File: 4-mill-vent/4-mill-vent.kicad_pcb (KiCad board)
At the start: 2 copper layers, 76.2 x 47.6 mm, 73 parts, among them J1 Fan, J2 Buzzer, J3 Power, J4 ICSP, Q1 MMBT3904, Q2 MMBT3904, Q3 PZT3904, Q4 PZT3904, Q5 TSM480P06CP, Q6 MMBT3904, SW1 Power_off, SW2 Power_On, SW3 Fan_Down, SW4 Fan_Up, U1 LM321, U2 TPSM84212EAB, U3 LM1117-5.0, U4 ATmega328P-AU, Y1 16.000MHZ

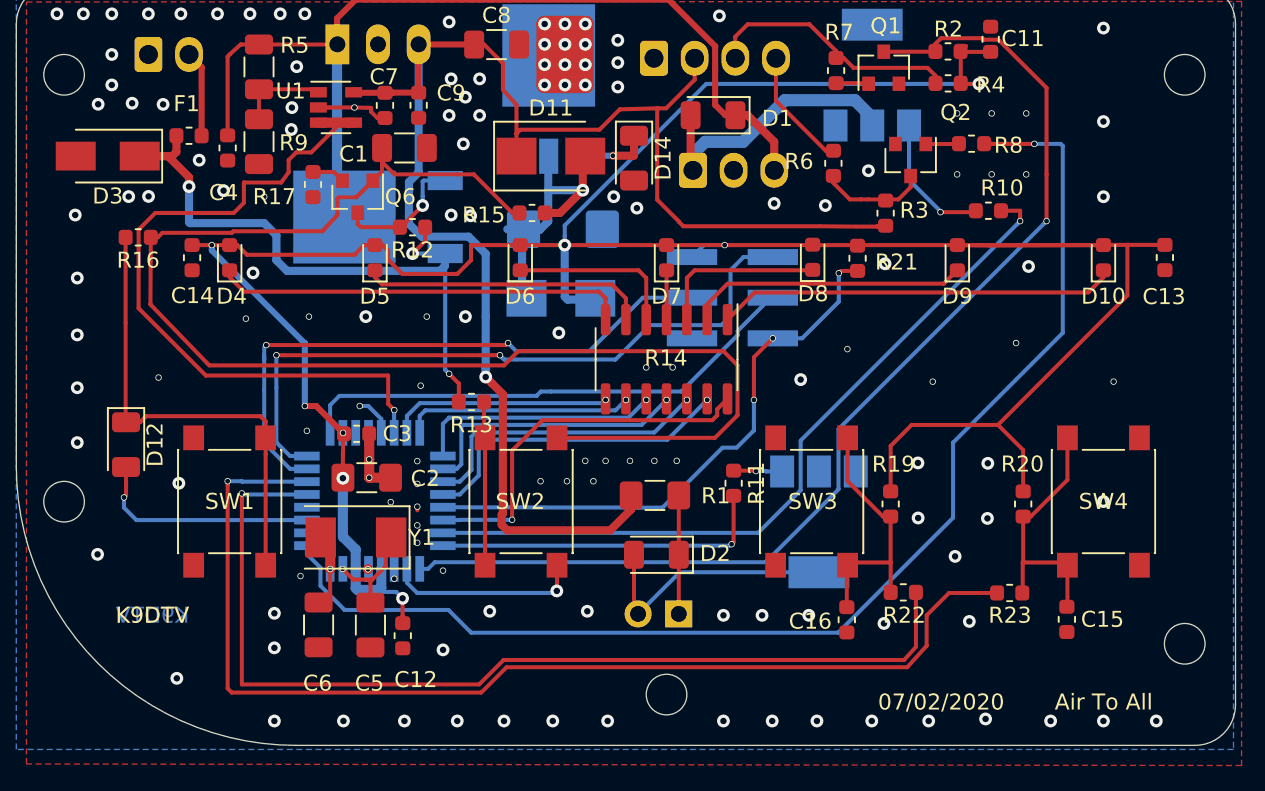
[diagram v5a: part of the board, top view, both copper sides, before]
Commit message: Added more to design
Had to add a transitor for allow the micro to power down the unit.
The reason is Q6's base can be as high as 16v when the on button is pressed.
This micro does not have open collector outputs and that would blow the chip.
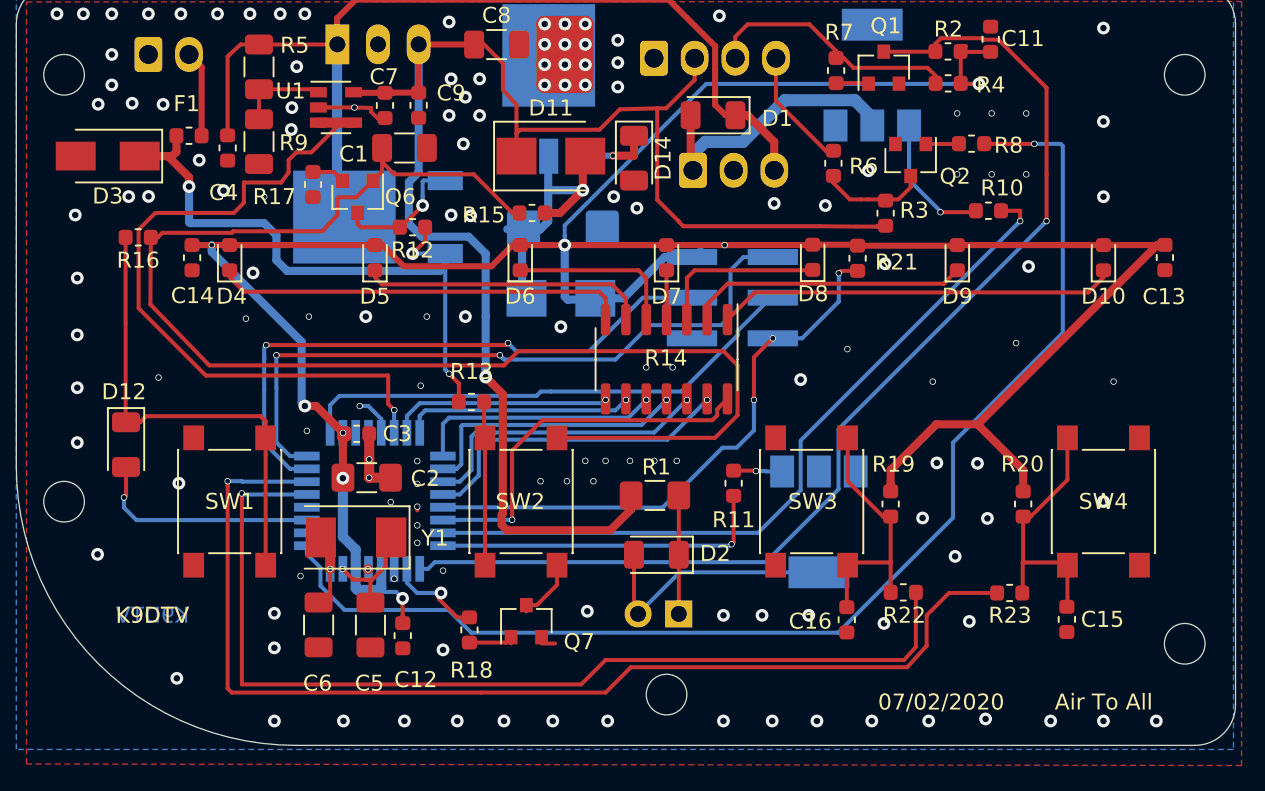
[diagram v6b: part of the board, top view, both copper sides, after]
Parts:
- added Q7: MMBT3904, Package_TO_SOT_SMD:SOT-23, F.Cu at (131.1, 108.2)
- added R18: 220k, Resistor_SMD:R_0603_1608Metric, F.Cu at (127.5, 108.7)
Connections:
- C7 pad 1: Monitor -> Net-(C7-Pad1)
- D12 pad 2: Micro_power_Down -> Monitor
- Q6 pad 1: Monitor -> Net-(C7-Pad1)
- R15 pad 1: Monitor -> Net-(C7-Pad1)
- R16 pad 1: Monitor -> Net-(C7-Pad1)
- SW2 pad 1: Monitor -> Net-(C7-Pad1)
- U4 pad 11: Micro_power_Down -> Monitor
- U4 pad 2: Monitor -> Micro_power_Down
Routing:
- net Net-(C7-Pad1): track 0.00 -> 91.0 mm
- net Monitor: track 99.4 -> 14.3 mm
- net +5V: track 178.6 -> 222.9 mm, vias 8 -> 9
- net Micro_power_Down: track 14.3 -> 6.07 mm
- net Net-(Q7-Pad1): track 0.00 -> 2.83 mm
- net GND: track 12.3 -> 13.1 mm
- net MOSI: vias 4 -> 3

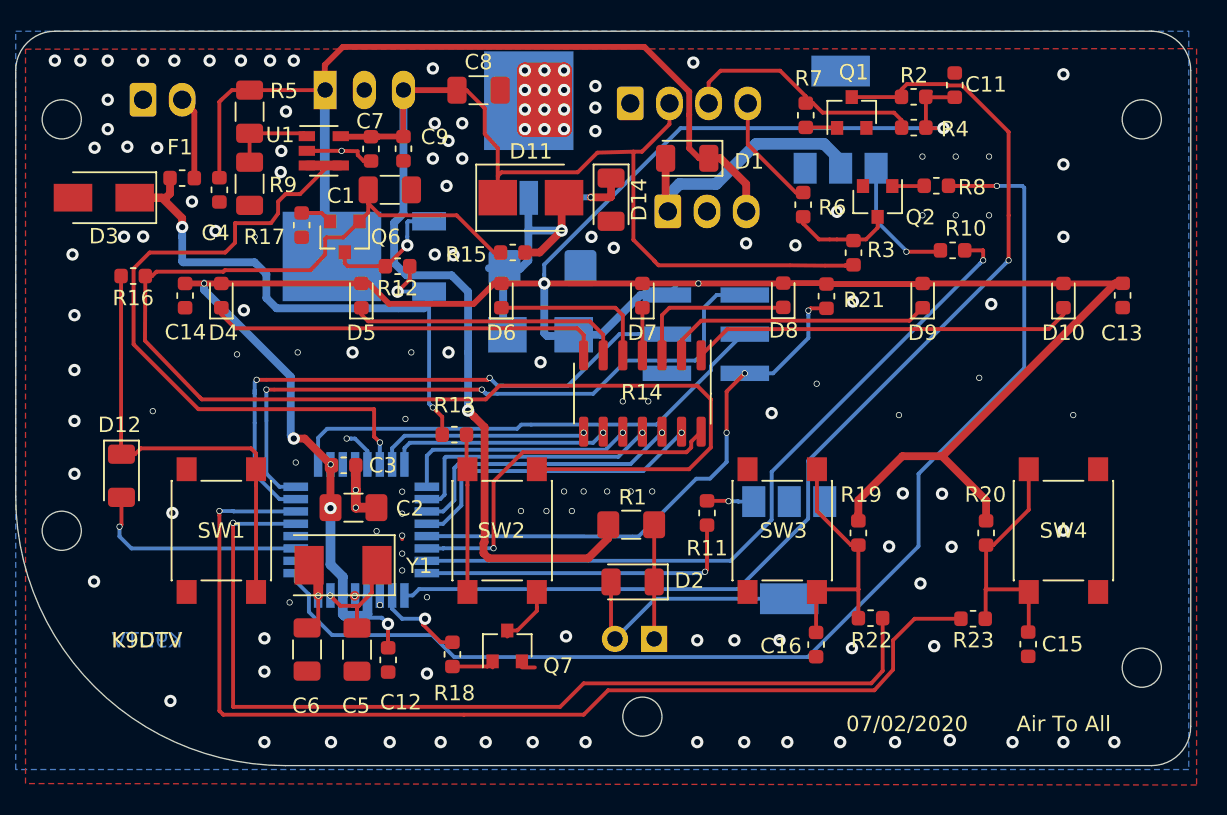
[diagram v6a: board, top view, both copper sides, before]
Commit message: Made debounce failsafe
found a missing resistor on raw rpm pull up. other little error or problems were fixed as well. all part of normal clean up
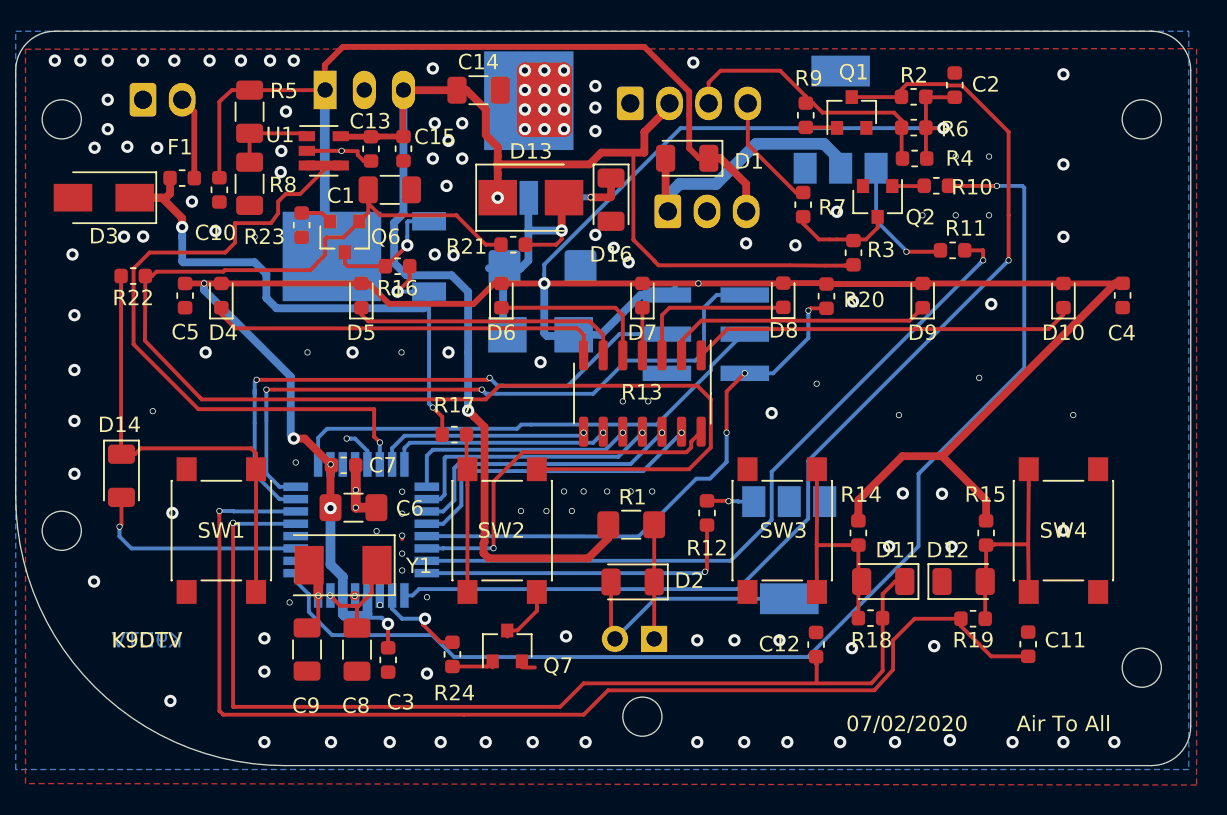
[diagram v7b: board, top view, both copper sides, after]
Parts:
- added D11: 1N914, Diode_SMD:D_1206_3216Metric, F.Cu at (155.4, 104.0)
- added D12: 1N914, Diode_SMD:D_1206_3216Metric, F.Cu at (160.7, 104.0)
- added R4: 10k, Resistor_SMD:R_0603_1608Metric, F.Cu at (157.5, 76.6)
- R24: renamed from R18; value 220k -> 4.7k
- R9: renamed from R7; value 10k -> 4.7k
- moved R21 0.51 mm to (131.4, 82.2)
- turned C11 to 90 degrees
- turned C12 to 90 degrees
- renumbered C4 to C10, C15 to C11, C16 to C12, C7 to C13, C8 to C14, C9 to C15, C10 to C16, C11 to C2, C12 to C3, C13 to C4, C14 to C5, C2 to C6, C3 to C7, C5 to C8, C6 to C9, D11 to D13, D12 to D14, D13 to D15, D14 to D16, R8 to R10, R10 to R11, R11 to R12, R14 to R13, R19 to R14, R20 to R15, R12 to R16, R13 to R17, R22 to R18, R23 to R19, R21 to R20, R15 to R21, R16 to R22, R17 to R23, R4 to R6, R6 to R7, R9 to R8, U4 to U2, U2 to U3, U3 to U4
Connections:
- C11 pad 1: Net-(C15-Pad1) -> Up
- C12 pad 1: Net-(C16-Pad1) (its old number) -> Down
- R14 pad 1: Net-(C16-Pad1) (its old number) -> Net-(D11-Pad2)
- R15 pad 1: Net-(C15-Pad1) -> Net-(D12-Pad2)
- R18 pad 1: Net-(C16-Pad1) (its old number) -> Net-(D11-Pad2)
- R19 pad 2: Net-(C15-Pad1) -> Net-(D12-Pad2)
- SW3 pad 2: Net-(C16-Pad1) (its old number) -> Net-(D11-Pad2)
- SW4 pad 2: Net-(C15-Pad1) -> Net-(D12-Pad2)
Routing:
- net Net-(C15-Pad1): track 16.6 -> 0.00 mm
- net Net-(C16-Pad1) (its old number): track 16.5 -> 0.00 mm
- net Net-(D11-Pad2): track 0.00 -> 15.7 mm
- net Net-(D12-Pad2): track 0.00 -> 15.5 mm
- net +12V: track 98.3 -> 107.2 mm, vias 1 -> 2
- net Up: track 69.8 -> 75.5 mm
- net Down: track 62.6 -> 67.6 mm
- net +5V: track 222.9 -> 224.9 mm
- net Raw_RPM: track 16.2 -> 18.3 mm
- net MOSI: vias 3 -> 2
- net GND: vias 128 -> 126

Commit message: more clean up
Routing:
- net GND: vias 126 -> 145
